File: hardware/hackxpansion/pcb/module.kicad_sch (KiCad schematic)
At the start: 3 parts

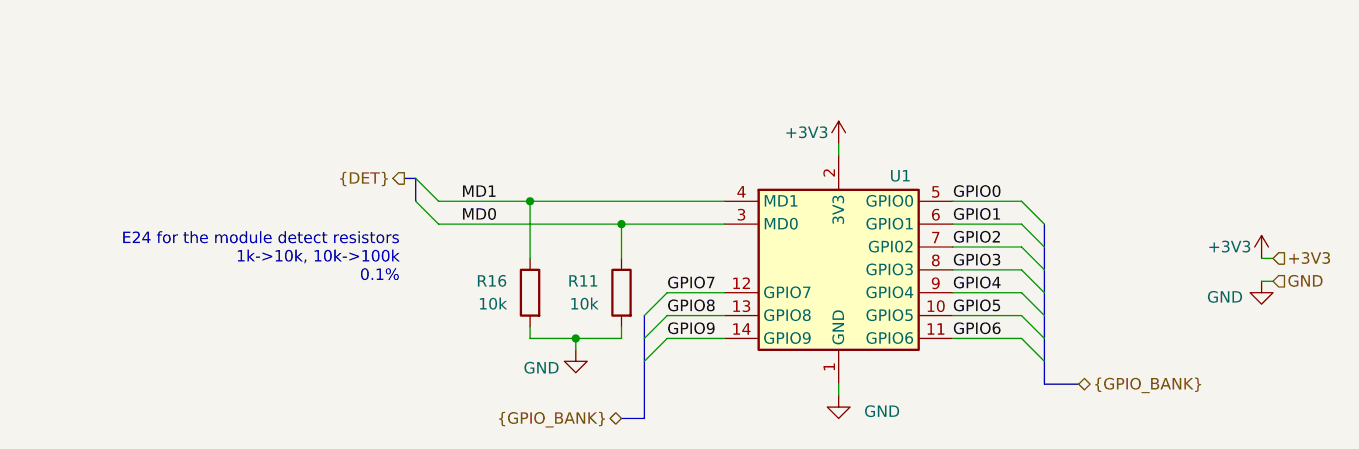
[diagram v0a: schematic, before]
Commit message: added series resistor to module power rail, so it can now do hotswap
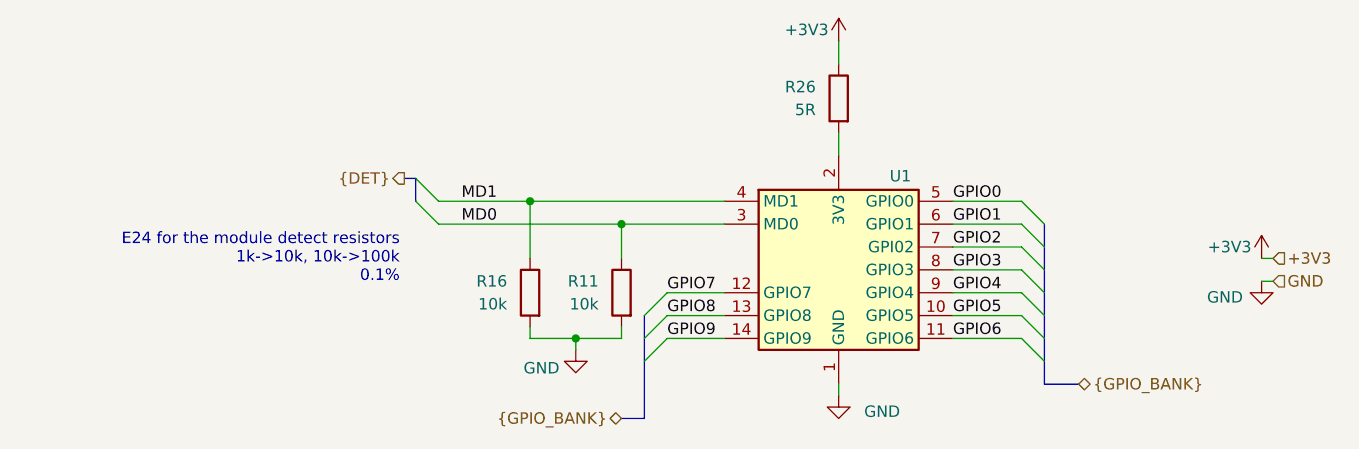
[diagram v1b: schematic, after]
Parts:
- added R26: 5R, Resistor_SMD:R_0402_1005Metric, symbol Device:R
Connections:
- net +3V3: now also R26.1; no longer U1.2 (3V3)
- new net: R26.2, U1.2 (3V3)
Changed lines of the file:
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@@
+	(wire
+		(pts
+			(xy 105.41 35.56) (xy 105.41 38.1)
+		)
+		(stroke
+			(width 0)
+			(type default)
+		)
+	)
 	(wire
 		(pts
@@
 		)
 	)
+	(wire
+		(pts
+			(xy 105.41 45.72) (xy 105.41 48.26)
+		)
+		(stroke
+			(width 0)
+			(type default)
+		)
+	)
 	(bus
 		(pts
@@
 		(pts
 			(xy 76.2 69.85) (xy 76.2 68.58)
-		)
-		(stroke
-			(width 0)
-			(type default)
-		)
-	)
-	(wire
-		(pts
-			(xy 105.41 46.99) (xy 105.41 48.26)
 		)
 		(stroke
@@
 		(lib_name "+3V3_1")
 		(lib_id "power:+3V3")
-		(at 105.41 46.99 0)
+		(at 105.41 35.56 0)
 		(unit 1)
 		(body_style 1)
@@
 		(dnp no)
 		(property "Reference" "#PWR057"
-			(at 105.41 50.8 0)
+			(at 105.41 39.37 0)
 			(hide yes)
 			(show_name no)
@@
 		)
 		(property "Value" "+3V3"
-			(at 101.854 45.72 0)
+			(at 101.854 34.29 0)
 			(show_name no)
 			(do_not_autoplace no)
@@
 		)
 		(property "Footprint" ""
-			(at 105.41 46.99 0)
+			(at 105.41 35.56 0)
 			(hide yes)
 			(show_name no)
@@
 		)
 		(property "Datasheet" ""
-			(at 105.41 46.99 0)
+			(at 105.41 35.56 0)
 			(hide yes)
 			(show_name no)
@@
 		)
 		(property "Description" "Power symbol creates a global label with name \"+3V3\""
-			(at 105.41 46.99 0)
+			(at 105.41 35.56 0)
 			(hide yes)
 			(show_name no)
@@
 					(unit 1)
 				)
+			)
+		)
+	)
+	(symbol
+		(lib_id "Device:R")
+		(at 105.41 41.91 0)
+		(mirror y)
+		(unit 1)
+		(body_style 1)
+		(exclude_from_sim no)
+		(in_bom yes)
+		(on_board yes)
+		(in_pos_files yes)
+		(dnp no)
+		(property "Reference" "R26"
+			(at 102.87 40.6399 0)
+			(show_name no)
+			(do_not_autoplace no)
+			(effects
+				(font
+					(size 1.27 1.27)
+				)
+				(justify left)
+			)
+		)
+		(property "Value" "5R"
+			(at 102.87 43.1799 0)
+			(show_name no)
+			(do_not_autoplace no)
+			(effects
+				(font
+					(size 1.27 1.27)
+				)
+				(justify left)
+			)
+		)
+		(property "Footprint" "Resistor_SMD:R_0402_1005Metric"
+			(at 107.188 41.91 90)
+			(hide yes)
+			(show_name no)
+			(do_not_autoplace no)
+			(effects
+				(font
+					(size 1.27 1.27)
+				)
+			)
+		)
+		(property "Datasheet" ""
+			(at 105.41 41.91 0)
+			(hide yes)
+			(show_name no)
+			(do_not_autoplace no)
+			(effects
+				(font
+					(size 1.27 1.27)
+				)
+			)
+		)
+		(property "Description" "Resistor"
+			(at 105.41 41.91 0)
+			(hide yes)
+			(show_name no)
+			(do_not_autoplace no)
+			(effects
+				(font
+					(size 1.27 1.27)
+				)
+			)
+		)
+		(property "LCSC" "C54920693"
+			(at 105.41 41.91 0)
+			(hide yes)
+			(show_name no)
+			(do_not_autoplace no)
+			(effects
+				(font
+					(size 1.27 1.27)
+				)
+			)
+		)
+		(pin "2"
+		)
+		(pin "1"
+		)
+		(instances
+			(project "hackxpansion"
+				(path "/aaf5804d-3f78-442b-969e-39faa388db94/61af021d-ad04-487f-9d02-e2b100ecd1ae/83610548-4b56-444f-89db-0bbc742f5add"
+					(reference "R27")
+					(unit 1)
+				)
+				(path "/aaf5804d-3f78-442b-969e-39faa388db94/61af021d-ad04-487f-9d02-e2b100ecd1ae/8e7c9aa8-528d-465c-8c66-453c45c0eb2c"
+					(reference "R26")
+					(unit 1)
+				)
+				(path "/aaf5804d-3f78-442b-969e-39faa388db94/7b3174ee-89a2-4fc3-aea9-d162748ee587/0547b68d-d760-4d9c-a3c3-9a4130f5ea65"
+					(reference "R28")
+					(unit 1)
+				)
+				(path "/aaf5804d-3f78-442b-969e-39faa388db94/7b3174ee-89a2-4fc3-aea9-d162748ee587/82bcf865-3cc6-4dae-b757-27ac9efd6517"
+					(reference "R29")
+					(unit 1)
+				)

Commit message: updated part numbers
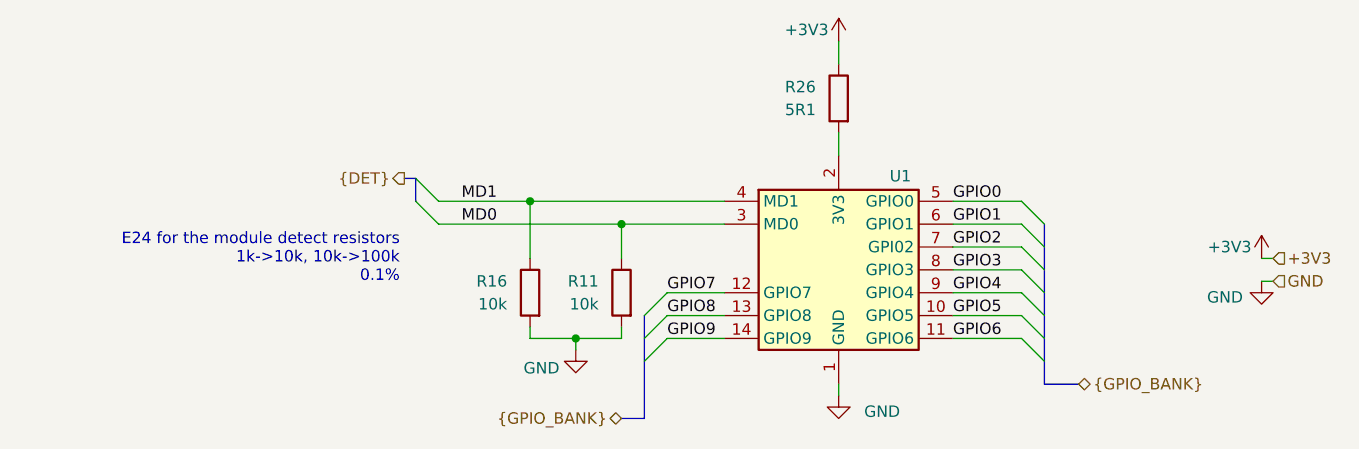
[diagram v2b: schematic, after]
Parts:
- R26: value 5R -> 5R1; LCSC C54920693 -> C2909363
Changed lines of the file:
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@@
 			)
 		)
-		(property "Value" "5R"
+		(property "Value" "5R1"
 			(at 102.87 43.1799 0)
 			(show_name no)
@@
 			)
 		)
-		(property "LCSC" "C54920693"
+		(property "LCSC" "C2909363"
 			(at 105.41 41.91 0)
 			(hide yes)

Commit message: updated module detect resistor to 0.1%
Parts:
- R11, R16: LCSC C2906861 -> C190095
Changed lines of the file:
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@@
 			)
 		)
-		(property "LCSC" "C2906861"
+		(property "LCSC" "C190095"
 			(at 81.28 63.5 0)
 			(hide yes)
@@
 			)
 		)
-		(property "LCSC" "C2906861"
+		(property "LCSC" "C190095"
 			(at 71.12 63.5 0)
 			(hide yes)
